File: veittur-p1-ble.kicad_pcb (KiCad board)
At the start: 2 copper layers, 40 x 20 mm, 19 parts, among them J1 Connector_HAN_P1, J2 Conn_01x06, Q1 BSS138, Q2 BSS138, U1 MIC5504-3.3YM5, U2 CH582F, Y1 32M, Y2 32k

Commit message: overhaul for jlc assembly
parts changes, revised layout, added the usb connector, just for fun...
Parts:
- added J1: USB_C_Receptacle_USB2.0, Connector_USB:USB_C_Receptacle_XKB_U262-16XN-4BVC11, F.Cu at (122.7, 99.5)
- added JP1: Jumper_2_Open, Connector_PinHeader_2.54mm:PinHeader_2x01_P2.54mm_Vertical, F.Cu at (130.6, 97.6)
- added R1: 10k, Resistor_SMD:R_0603_1608Metric, F.Cu at (125.2, 92.8)
- added R2: 10k, Resistor_SMD:R_0603_1608Metric, F.Cu at (123.7, 92.8)
- added R3: 10k, Resistor_SMD:R_0603_1608Metric, F.Cu at (120.7, 92.8)
- added R4: 10k, Resistor_SMD:R_0603_1608Metric, F.Cu at (122.2, 92.8)
- added R7: 0, Resistor_SMD:R_0603_1608Metric, F.Cu at (128.8, 85.0)
- added SW1: SW_Push, Connector_PinHeader_1.27mm:PinHeader_2x01_P1.27mm_Vertical, F.Cu at (132.3, 95.2)
- added TP2: TestPoint, TestPoint:TestPoint_Pad_1.0x1.0mm, F.Cu at (116.8, 90.5)
- added TP3: TestPoint, TestPoint:TestPoint_Pad_1.0x1.0mm, F.Cu at (121.6, 81.3)
- D1: value WS2812C-2020 -> WS2812B-V5/W; footprint LED_SMD:LED_WS2812-2020-PLCC4_2.0x2.0mm -> LED_SMD:LED_WS2812B_PLCC4_5.0x5.0mm_P3.2mm
- L1: footprint Inductor_SMD:L_0805_2012Metric -> et-parts:L_Changjiang_FNR252012S
- moved J3 15.6 mm to (115.5, 100.2)
- moved D1 6.80 mm to (114.0, 80.7), turned to 180 degrees
- moved Y2 4.31 mm to (119.7, 83.3)
- moved C5 3.94 mm to (120.0, 89.6)
- moved C4 3.70 mm to (118.3, 87.0)
- moved C2 3.69 mm to (116.8, 87.0)
- moved L1 3.69 mm to (120.4, 87.0)
- moved C3 3.06 mm to (126.5, 82.9)
- moved U2 3.06 mm to (125.0, 87.5)
- moved J2 3.00 mm to (107.3, 89.5)
- moved C1 1.94 mm to (111.2, 94.0)
- moved U1 1.94 mm to (114.2, 94.0)
- moved R5 1.91 mm to (114.9, 85.7)
- moved R6 1.91 mm to (114.9, 89.7)
- moved Q1 1.91 mm to (112.3, 85.7)
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- renumbered J1 to J2, J2 to J3, R1 to R5, R2 to R6
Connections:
- net Net-(C6-Pad1) renamed /vinta
- net Net-(U2-Pad1) renamed /x32o
- net Net-(U2-Pad18) renamed /clko
- net Net-(U2-Pad19) renamed /clki
- net Net-(U2-Pad2) renamed /x32i
- U2 pad 12: unconnected-(U2-Pad12) -> /USBP
- U2 pad 13: unconnected-(U2-Pad13) -> /USBN
- U2 pad 16: unconnected-(U2-Pad16) -> /RST
- U2 pad 21: Net-(AE1-Pad1) -> Net-(R7-Pad2)
- U2 pad 24: /LED_OUT3V3 -> unconnected-(U2-Pad24)
- U2 pad 25: /P1_DATA -> unconnected-(U2-Pad25)
- U2 pad 26: unconnected-(U2-Pad26) -> /LED_OUT3V3
- U2 pad 28: unconnected-(U2-Pad28) -> /P1_REQ_OUT
- U2 pad 6: unconnected-(U2-Pad6) -> /P1_DATA
- U2 pad 7: /P1_REQ_OUT -> unconnected-(U2-Pad7)
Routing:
- net /U_TX: track 6.85 -> 35.5 mm
- net /U_RX: track 8.11 -> 32.9 mm
- net +5V: track 45.8 -> 65.9 mm, vias 0 -> 1
- net /USBN: track 0.00 -> 18.7 mm
- net /USBP: track 0.00 -> 18.6 mm
- net /TIO: track 7.07 -> 25.3 mm
- net /vbus: track 0.00 -> 18.2 mm, vias 0 -> 2
- net /TCK: track 8.78 -> 26.5 mm
- net /RST: track 0.00 -> 9.25 mm
- net /LED_OUT3V3: track 9.55 -> 18.3 mm
- net /P1_REQ_OUT: track 16.4 -> 22.7 mm
- net Net-(AE1-Pad1): track 10.8 -> 5.61 mm
- net /cc2: track 0.00 -> 3.87 mm
- net /cc1: track 0.00 -> 3.87 mm
- net /clko: track 5.86 -> 8.98 mm
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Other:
- board size 40 x 20 mm -> 40 x 24 mm

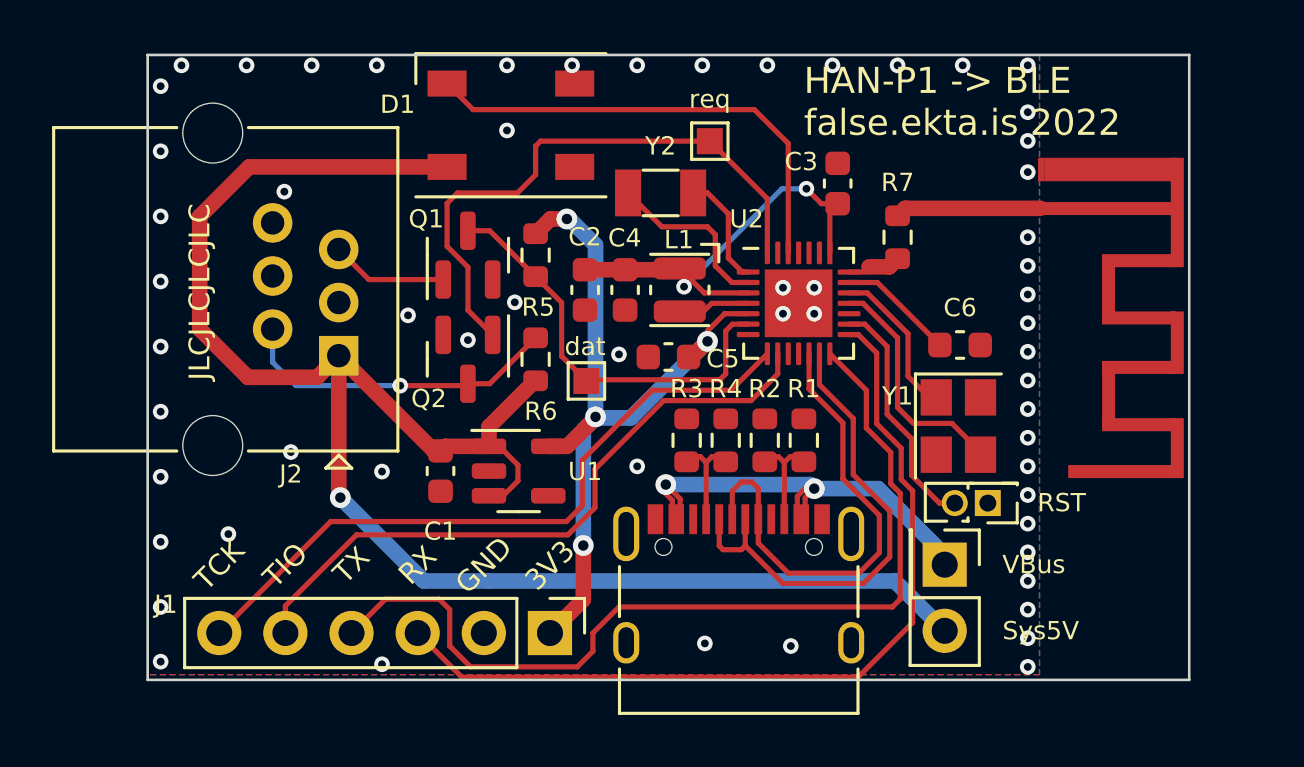
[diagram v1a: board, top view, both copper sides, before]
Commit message: finalize production for rev2.
parts all adjusted for JLCPCB, bom and position files all uploaded
happily.
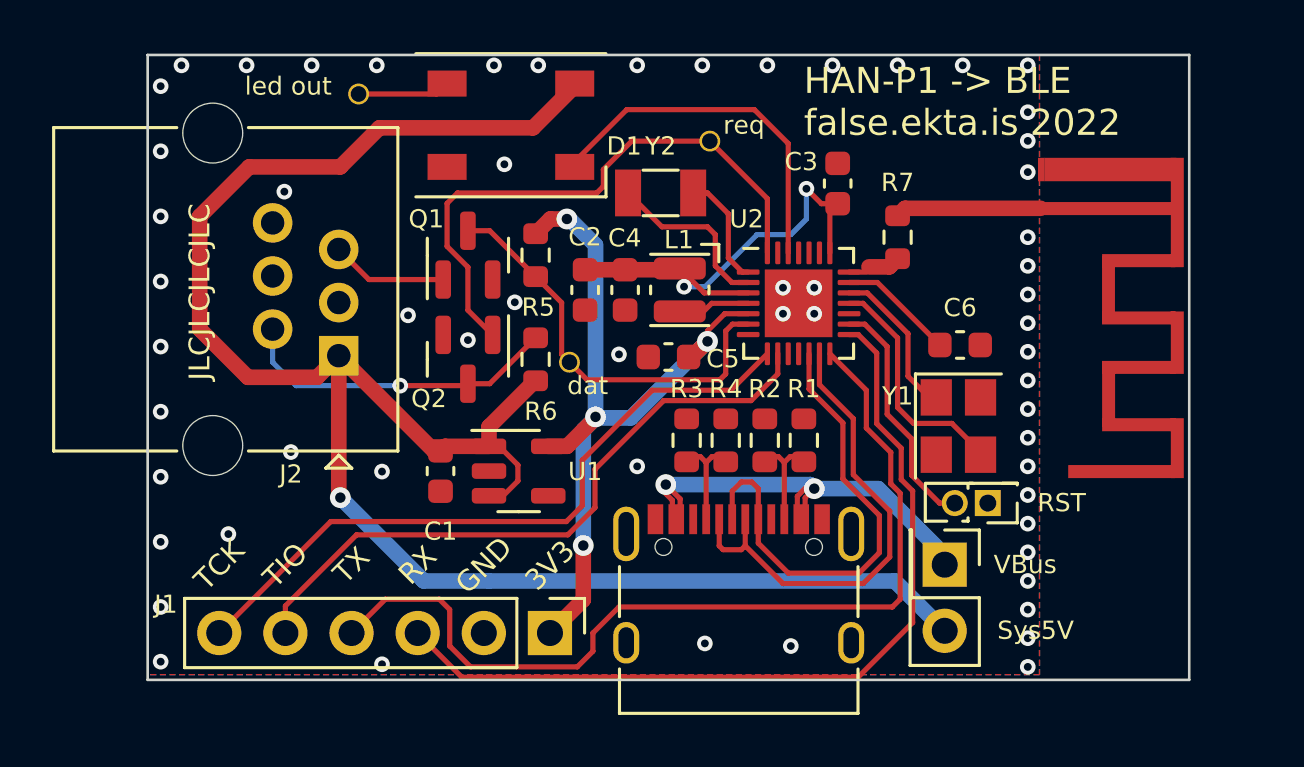
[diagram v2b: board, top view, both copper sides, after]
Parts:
- added TP3: TestPoint, et-parts:TestPoint_Plated_Hole_0.6_D0.8mm, F.Cu at (108.1, 79.5)
- TP1: renamed from TP2; footprint TestPoint:TestPoint_Pad_1.0x1.0mm -> et-parts:TestPoint_Plated_Hole_0.6_D0.8mm
- TP2: renamed from TP3; footprint TestPoint:TestPoint_Pad_1.0x1.0mm -> et-parts:TestPoint_Plated_Hole_0.6_D0.8mm
- moved TP1 0.97 mm to (116.2, 89.8)
- turned D1 to 0 degrees
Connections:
- D1 pad 1: unconnected-(D1-Pad1) -> Net-(D1-Pad1)
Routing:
- net +5V: track 65.9 -> 72.1 mm
- net /LED_OUT3V3: track 18.3 -> 14.0 mm
- net Net-(D1-Pad1): track 0.00 -> 3.57 mm
- net /VDCIx: track 17.4 -> 18.1 mm
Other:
- board text added: "dat"
- board text added: "led out"
- board text added: "req"
